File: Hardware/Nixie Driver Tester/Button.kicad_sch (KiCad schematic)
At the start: 3 parts, among them SW1 SW_Omron_B3FS

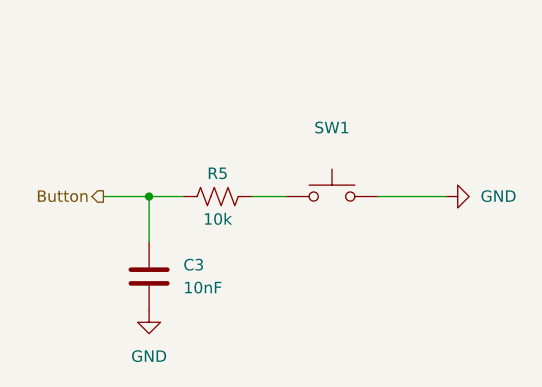
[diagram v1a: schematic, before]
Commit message: Switch mode 3.3V and SMD inductor
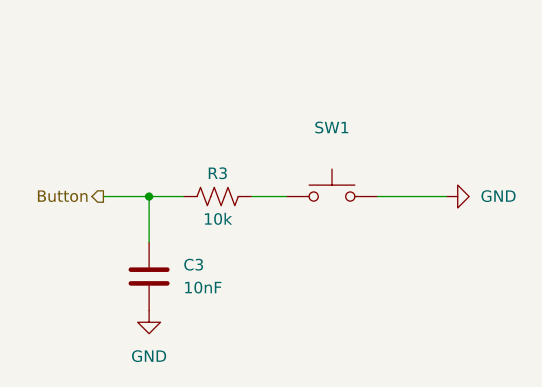
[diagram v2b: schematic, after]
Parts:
- renumbered R5 to R3
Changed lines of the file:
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@@
 		(dnp no)
 		(fields_autoplaced yes)
-		(property "Reference" "#PWR03"
+		(property "Reference" "#PWR09"
 			(at 119.38 107.95 0)
 			(hide yes)
@@
 			(project "Nixie Driver Tester"
 				(path "/c2082ee6-4c2e-4b3c-b2d7-410eae192cfe/6e79d909-830f-4059-b641-0b140124ed9d"
-					(reference "#PWR03")
+					(reference "#PWR09")
 					(unit 1)
 				)
@@
 		(in_pos_files yes)
 		(dnp no)
-		(property "Reference" "R5"
+		(property "Reference" "R3"
 			(at 127 86.36 90)
 			(show_name no)
@@
 			(project "Nixie Driver Tester"
 				(path "/c2082ee6-4c2e-4b3c-b2d7-410eae192cfe/6e79d909-830f-4059-b641-0b140124ed9d"
-					(reference "R5")
+					(reference "R3")
 					(unit 1)
 				)
@@
 		(dnp no)
 		(fields_autoplaced yes)
-		(property "Reference" "#PWR013"
+		(property "Reference" "#PWR010"
 			(at 158.75 88.9 0)
 			(hide yes)
@@
 			(project "Nixie Driver Tester"
 				(path "/c2082ee6-4c2e-4b3c-b2d7-410eae192cfe/6e79d909-830f-4059-b641-0b140124ed9d"
-					(reference "#PWR013")
+					(reference "#PWR010")
 					(unit 1)
 				)

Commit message: Added test points
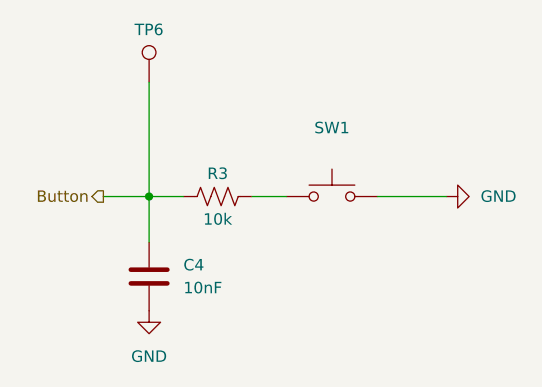
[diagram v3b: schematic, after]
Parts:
- added TP6: BTN, TestPoint:TestPoint_Keystone_5015_Micro_Mini, symbol Connector:TestPoint
- renumbered C3 to C4
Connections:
- net Button: now also TP6.1
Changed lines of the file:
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@@
+	(wire
+		(pts
+			(xy 119.38 76.2) (xy 119.38 88.9)
+		)
+		(stroke
+			(width 0)
+			(type default)
+		)
+	)
 	(wire
 		(pts
@@
 		(dnp no)
 		(fields_autoplaced yes)
-		(property "Reference" "#PWR09"
+		(property "Reference" "#PWR010"
 			(at 119.38 107.95 0)
 			(hide yes)
@@
 			(project "Nixie Driver Tester"
 				(path "/c2082ee6-4c2e-4b3c-b2d7-410eae192cfe/6e79d909-830f-4059-b641-0b140124ed9d"
-					(reference "#PWR09")
+					(reference "#PWR010")
 					(unit 1)
 				)
@@
 		(dnp no)
 		(fields_autoplaced yes)
-		(property "Reference" "#PWR010"
+		(property "Reference" "#PWR011"
 			(at 158.75 88.9 0)
 			(hide yes)
@@
 			(project "Nixie Driver Tester"
 				(path "/c2082ee6-4c2e-4b3c-b2d7-410eae192cfe/6e79d909-830f-4059-b641-0b140124ed9d"
-					(reference "#PWR010")
+					(reference "#PWR011")
 					(unit 1)
 				)
@@
 		(dnp no)
 		(fields_autoplaced yes)
-		(property "Reference" "C3"
+		(property "Reference" "C4"
 			(at 123.19 96.5199 0)
 			(show_name no)
@@
 			(project "Nixie Driver Tester"
 				(path "/c2082ee6-4c2e-4b3c-b2d7-410eae192cfe/6e79d909-830f-4059-b641-0b140124ed9d"
-					(reference "C3")
+					(reference "C4")
 					(unit 1)
 				)
+			)
+		)
+	)
+	(symbol
+		(lib_id "Connector:TestPoint")
+		(at 119.38 76.2 0)
+		(unit 1)
+		(body_style 1)
+		(exclude_from_sim no)
+		(in_bom yes)
+		(on_board yes)
+		(in_pos_files yes)
+		(dnp no)
+		(property "Reference" "TP6"
+			(at 119.38 71.12 0)
+			(show_name no)
+			(do_not_autoplace no)
+			(effects
+				(font
+					(size 1.27 1.27)
+				)
+				(justify bottom)
+			)
+		)
+		(property "Value" "BTN"
+			(at 121.92 74.1679 0)
+			(hide yes)
+			(show_name no)
+			(do_not_autoplace no)
+			(effects
+				(font
+					(size 1.27 1.27)
+				)
+				(justify left)
+			)
+		)
+		(property "Footprint" "TestPoint:TestPoint_Keystone_5015_Micro_Mini"
+			(at 124.46 76.2 0)
+			(hide yes)
+			(show_name no)
+			(do_not_autoplace no)
+			(effects
+				(font
+					(size 1.27 1.27)
+				)
+			)
+		)
+		(property "Datasheet" ""
+			(at 124.46 76.2 0)
+			(hide yes)
+			(show_name no)
+			(do_not_autoplace no)
+			(effects
+				(font
+					(size 1.27 1.27)
+				)
+			)
+		)
+		(property "Description" "test point"
+			(at 119.38 76.2 0)
+			(hide yes)
+			(show_name no)
+			(do_not_autoplace no)
+			(effects
+				(font
+					(size 1.27 1.27)
+				)
+			)
+		)
+		(pin "1"
+		)
+		(instances
+			(project "Nixie Driver Tester"
+				(path "/c2082ee6-4c2e-4b3c-b2d7-410eae192cfe/6e79d909-830f-4059-b641-0b140124ed9d"
+					(reference "TP6")
+					(unit 1)
+				)
